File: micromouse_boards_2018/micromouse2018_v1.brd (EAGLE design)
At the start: 100 x 80 mm, 57 parts, among them IC1 TPS562210DDFT

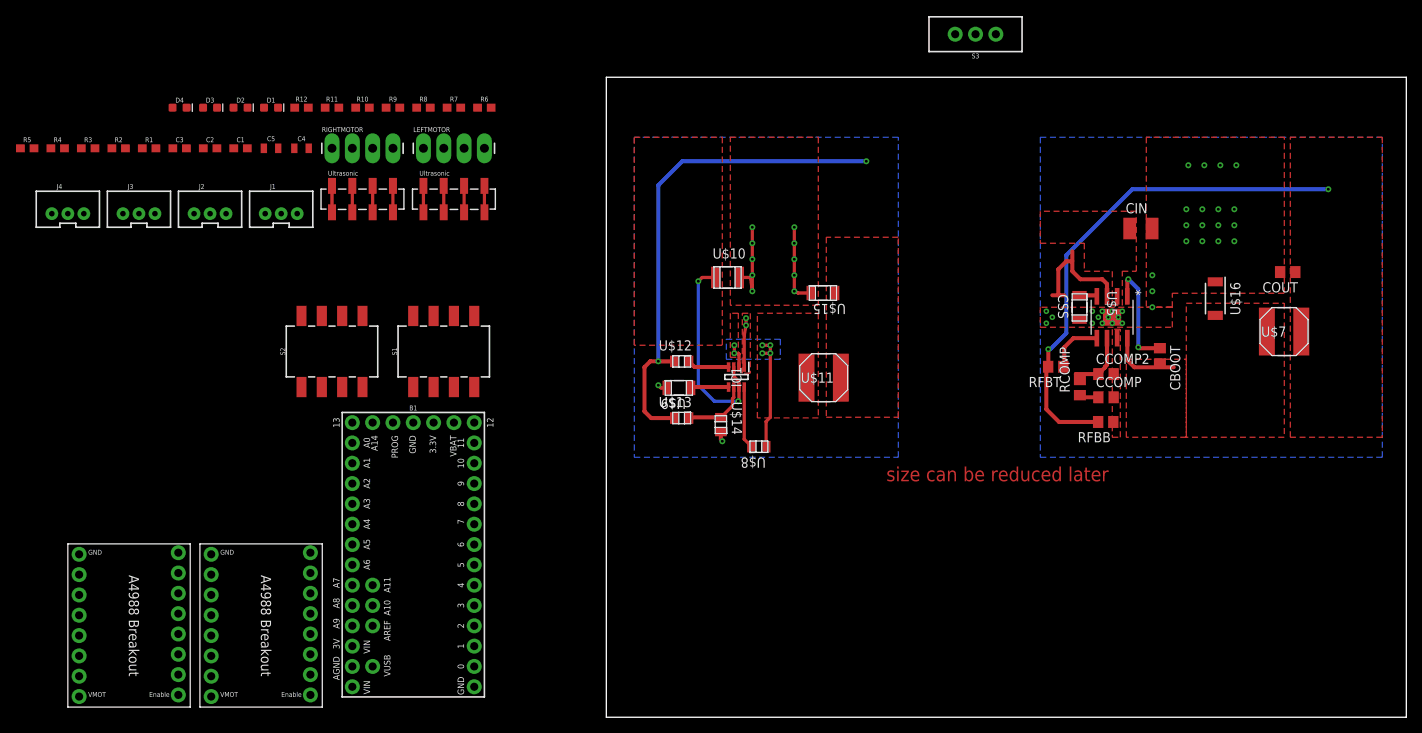
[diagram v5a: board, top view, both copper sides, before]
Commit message: Completed Board layout, passed DRC, removed 2 status LEDs, increased C6 C7
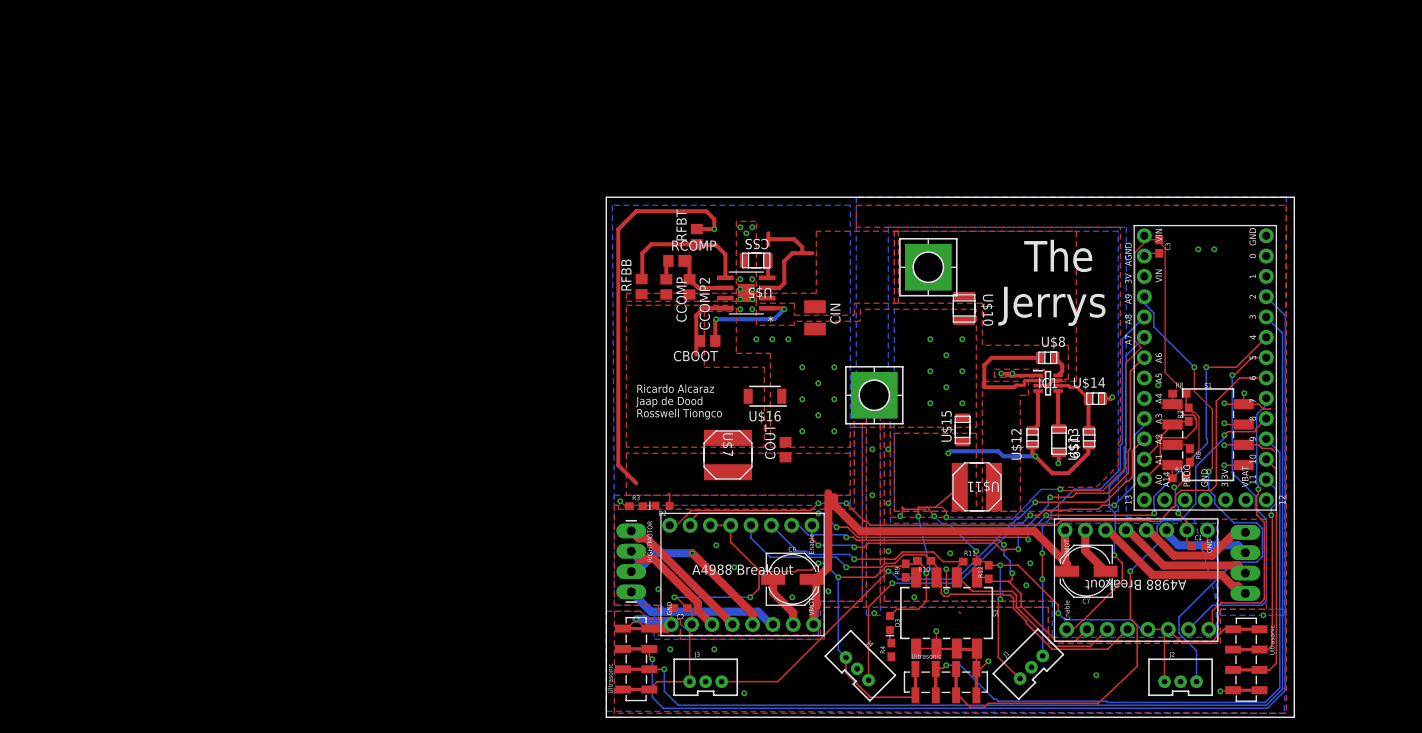
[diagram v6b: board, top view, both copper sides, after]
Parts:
- removed C4, C5: 1.0uF, SparkFun-Capacitors:0805
- removed D1, D4: (no value), SparkFun-LED:LED-0603
- removed R2: 1k, SparkFun-Resistors:0603
- removed R5: 330, SparkFun-Resistors:0603
- removed S3: (no value), SparkFun-Switches:SWITCH_SPDT_PTH_11.6X4.0MM
- added C6, C7: 100uF, SparkFun-Capacitors:PANASONIC_D
- added GND, H1: MOUNT-PAD-SQUARE3.6, holes:3,6-PAD-SQUARE
- added U$6: ULTRASONIC, raParts:1X04_SMD_VERTICAL_COMBO
- moved FRAME1 182.4 mm to (101.2, 73.3)
- moved R1 135.2 mm to (71.6, 29.9)
- moved J2 134.7 mm to (71.8, 5.00)
- moved C1 129.7 mm to (74.0, 21.4)
- moved C3 123.1 mm to (69.1, 58.8), turned to 270 degrees
- moved R4 121.6 mm to (35.6, 8.42), turned to 90 degrees
- moved J4 114.3 mm to (31.8, 6.44), turned to 315 degrees
- moved LEFTMOTOR 113.4 mm to (79.9, 23.1), flipped to the bottom, turned to 270 degrees
- moved U$1 109.4 mm to (56.0, 24.8), turned to 270 degrees
- moved J1 109.3 mm to (52.8, 6.64), turned to 45 degrees
- moved D3 106.6 mm to (35.5, 11.8), turned to 270 degrees
- moved R12 103.7 mm to (47.8, 18.1), turned to 90 degrees
- moved B1 101.7 mm to (74.9, 43.7), flipped to the bottom, turned to 180 degrees
- moved R8 101.0 mm to (71.6, 40.5)
- moved R7 99.5 mm to (72.8, 37.8), turned to 90 degrees
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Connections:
- removed net DIRECTION: U$2.DIRECTION
- removed net N$1: D1.A, R2.2
- removed net N$4: D4.A, R5.2
- removed net VUSB: B1.VUSB
- removed net V_BATT: D1.C, S3.3
- new net ECHO3: B1.10, U$6.3, U$6.3-2
- new net TRIG3: B1.11, U$6.2, U$6.2-2
- net 12V: now also C6.+, C7.+, D2.A; no longer C4.1, C5.1, D2.C
- net 3.3V: no longer D4.C
- net 5V: now also D3.A, U$6.1, U$6.1-2; no longer D3.C
- net DIRECTION1: now also B1.6, U$2.DIRECTION; no longer B1.7
- net DIRECTION2: now also B1.7; no longer B1.8
- net ECHO1: now also B1.8
- net ECHO2: now also B1.2
- net GND: now also C6.-, C7.-, U$6.4, U$6.4-2; no longer C4.2, C5.2, R2.1, R5.1, S3.1
- net N$2: now also D2.C; no longer D2.A
- net N$3: now also D3.C; no longer D3.A
- net STEP1: now also B1.4; no longer B1.3
- net STEP2: now also B1.5; no longer B1.4
- net TRIG1: now also B1.9
- net TRIG2: now also B1.3
- net VIN: now also H1.B3,6; no longer S3.2
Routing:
- net 5V: track 63.0 -> 316.6 mm, vias 2 -> 18
- net ECHO2: track 0.00 -> 140.3 mm, vias 0 -> 1
- net TRIG2: track 0.00 -> 134.1 mm, vias 0 -> 1
- net STEP1: track 0.00 -> 92.3 mm, vias 0 -> 6
- net DIRECTION1: track 0.00 -> 91.6 mm, vias 0 -> 2
- net TRIG1: track 0.00 -> 80.9 mm, vias 0 -> 1
- net ECHO1: track 0.00 -> 70.2 mm, vias 0 -> 2
- net VO3: track 0.00 -> 68.3 mm, vias 0 -> 2
- net ENABLE1: track 0.00 -> 63.4 mm, vias 0 -> 4
- net GND: track 29.8 -> 93.2 mm, vias 47 -> 69
- net VO2: track 0.00 -> 63.2 mm, vias 0 -> 2
- net MS3: track 0.00 -> 60.3 mm, vias 0 -> 1
- net VO4: track 0.00 -> 57.5 mm, vias 0 -> 3
- net 12V: track 50.9 -> 107.7 mm, vias 2 -> 1
- net MS2: track 0.00 -> 53.0 mm, vias 0 -> 1
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- removed copper zone on layer 16, net BOOT
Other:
- board size 100 x 80 mm -> 86 x 65 mm
- board text added: "Ricardo Alcaraz Jaap de Dood Rosswell Tiongco"
- board text added: "The Jerrys"
- board text removed: "size can be reduced later"

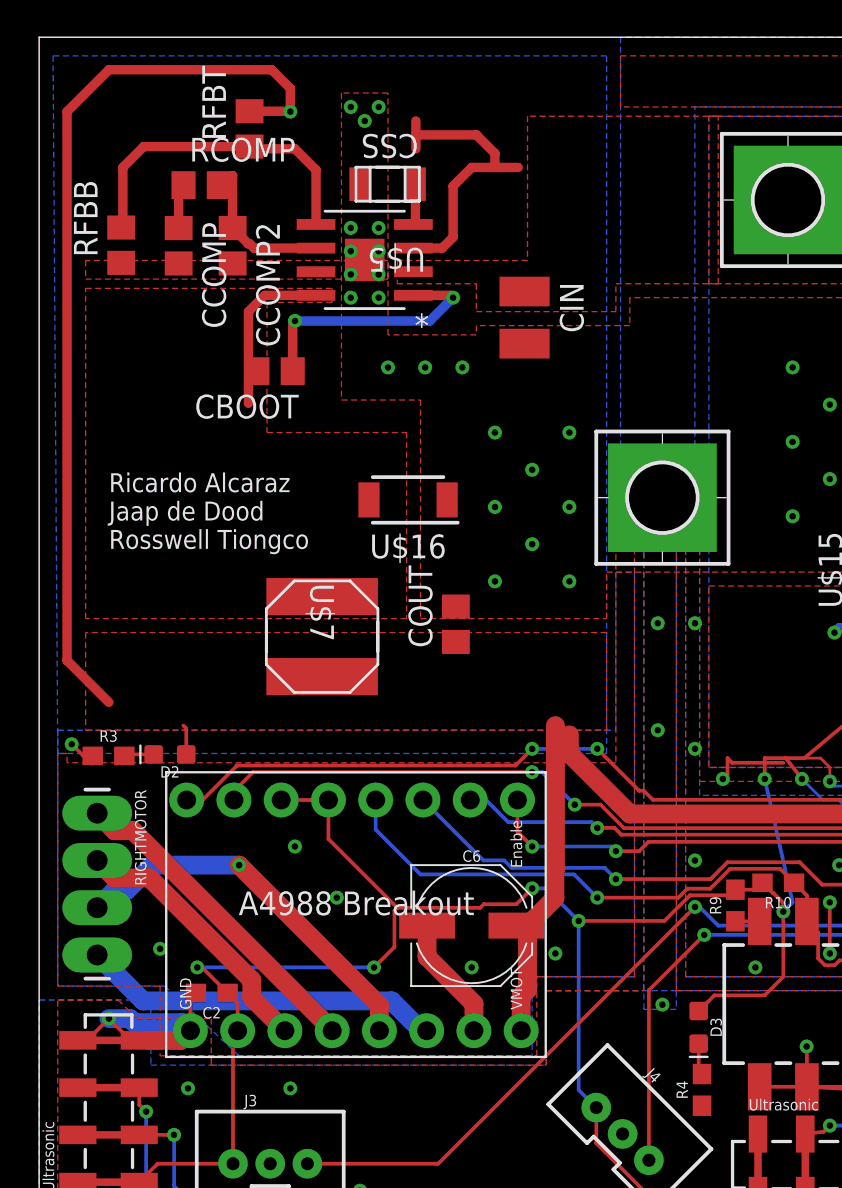
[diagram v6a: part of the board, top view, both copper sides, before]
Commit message: Fixed some silkscreen labels
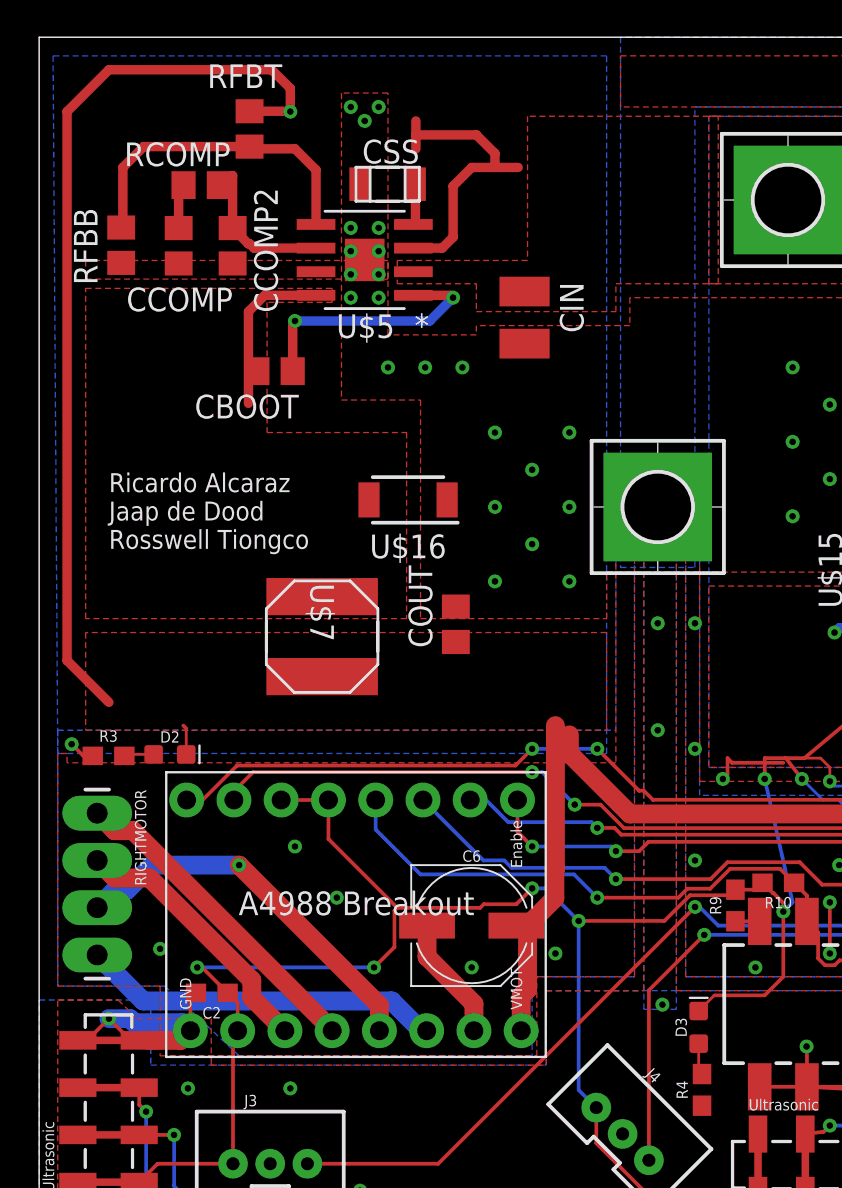
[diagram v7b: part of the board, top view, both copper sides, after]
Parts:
- removed GND: MOUNT-PAD-SQUARE3.6, holes:3,6-PAD-SQUARE
- added H2: MOUNT-PAD-SQUARE3.6, holes:3,6-PAD-SQUARE
- turned D2 to 0 degrees
- turned D3 to 90 degrees
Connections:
- removed net N$3: D3.C, R4.2
- new net N$1: D2.A, R3.2
- net 12V: now also D2.C; no longer D2.A
- net 5V: now also D3.C; no longer D3.A
- net GND: now also H2.B3,6
- net N$2: now also D3.A, R4.2; no longer D2.C, R3.2
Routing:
- net N$3: track 1.71 -> 0.00 mm
- net N$1: track 0.00 -> 1.61 mm
